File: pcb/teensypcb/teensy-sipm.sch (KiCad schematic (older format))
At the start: 14 parts, among them IC1 LF347D, IC2 L298, P1 CONN_5, P2 CONN_5, P3 CONN_14, P4 CONN_14, P5 CONN_1, U1 TEENSY3

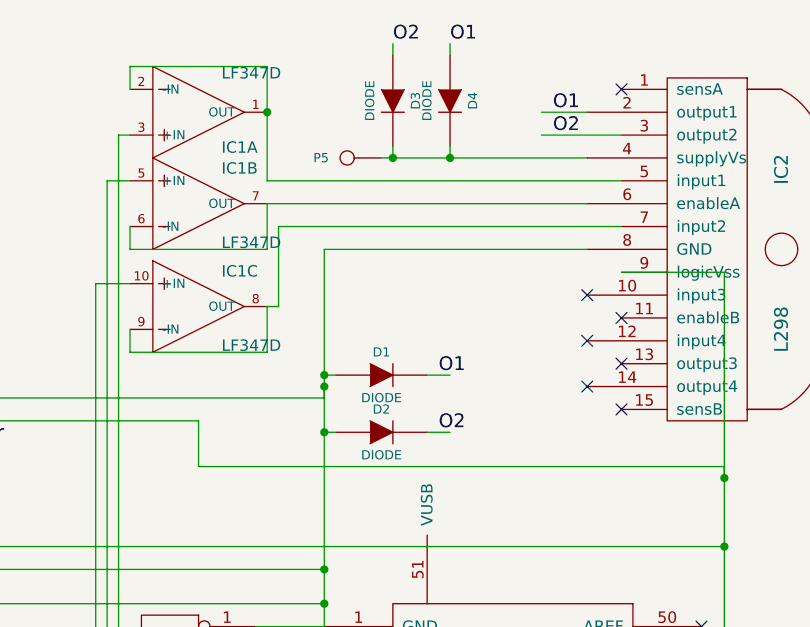
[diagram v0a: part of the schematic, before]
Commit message: SiPM Light readings -- not good
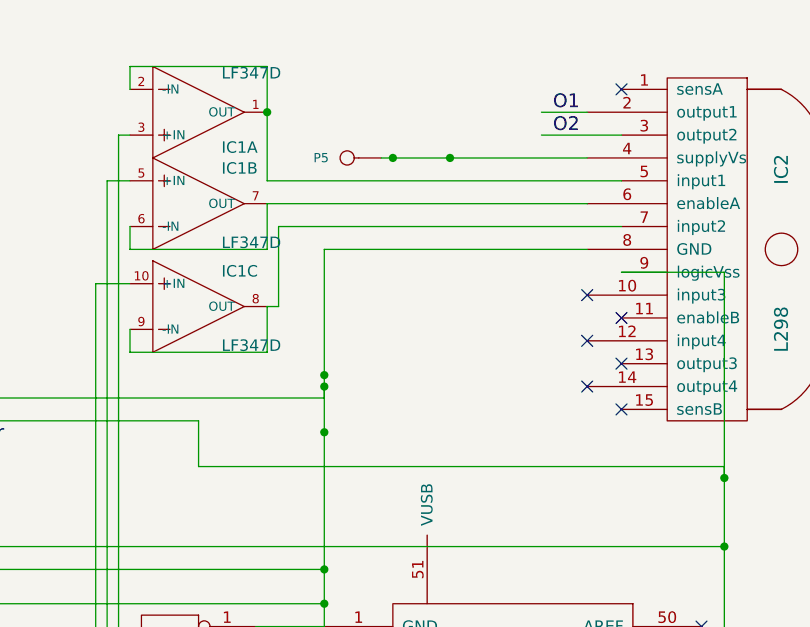
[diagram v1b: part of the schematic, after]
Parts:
- removed D1, D2, D3, D4: DIODE, ~, symbol DIODE
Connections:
- wire segments 110 -> 102
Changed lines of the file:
@@
 LIBS:sma_edge
 LIBS:l298
+LIBS:teensy-sipm-cache
 EELAYER 27 0
 EELAYER END
@@
 $EndComp
 $Comp
-L DIODE D1
-U 1 1 5338B550
-P 4650 1950
-F 0 "D1" H 4650 2050 40  0000 C CNN
-F 1 "DIODE" H 4650 1850 40  0000 C CNN
-F 2 "~" H 4650 1950 60  0000 C CNN
-F 3 "~" H 4650 1950 60  0000 C CNN
-	1    4650 1950
-	1    0    0    -1
-$EndComp
-$Comp
-L DIODE D2
-U 1 1 5338B55D
-P 4650 2200
-F 0 "D2" H 4650 2300 40  0000 C CNN
-F 1 "DIODE" H 4650 2100 40  0000 C CNN
-F 2 "~" H 4650 2200 60  0000 C CNN
-F 3 "~" H 4650 2200 60  0000 C CNN
-	1    4650 2200
-	1    0    0    -1
-$EndComp
-$Comp
-L DIODE D3
-U 1 1 5338B563
-P 4700 750
-F 0 "D3" H 4700 850 40  0000 C CNN
-F 1 "DIODE" H 4700 650 40  0000 C CNN
-F 2 "~" H 4700 750 60  0000 C CNN
-F 3 "~" H 4700 750 60  0000 C CNN
-	1    4700 750
-	0    1    1    0
-$EndComp
-$Comp
-L DIODE D4
-U 1 1 5338B569
-P 4950 750
-F 0 "D4" H 4950 850 40  0000 C CNN
-F 1 "DIODE" H 4950 650 40  0000 C CNN
-F 2 "~" H 4950 750 60  0000 C CNN
-F 3 "~" H 4950 750 60  0000 C CNN
-	1    4950 750
-	0    1    1    0
-$EndComp
-$Comp
 L CONN_1 P5
 U 1 1 5338B571
@@
 Text Label 5400 900  0    60   ~ 0
 O2
-Text Label 4950 500  0    60   ~ 0
-O1
-Text Label 4700 500  0    60   ~ 0
-O2
-Text Label 4900 1950 0    60   ~ 0
-O1
-Text Label 4900 2200 0    60   ~ 0
-O2
 $Comp
 L CONN_5 P1
@@
 Wire Wire Line
 	4650 1000 5550 1000
-Wire Wire Line
-	4450 1950 4400 1950
 Connection ~ 4400 1950
-Wire Wire Line
-	4400 2200 4450 2200
 Connection ~ 4400 2200
-Wire Wire Line
-	4700 950  4700 1000
 Connection ~ 4700 1000
-Wire Wire Line
-	4950 950  4950 1000
 Connection ~ 4950 1000
 Wire Wire Line
-	4950 550  4950 500
-Wire Wire Line
-	4700 550  4700 500
-Wire Wire Line
-	4850 1950 4950 1950
-Wire Wire Line
-	4850 2200 4950 2200
-Wire Wire Line
 	5350 900  5700 900
